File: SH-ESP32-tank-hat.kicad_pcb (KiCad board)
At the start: 2 copper layers, 34 x 58 mm, 50 parts, among them J301 I2C_top, J302 I2C_bottom, J303 GPIO subset, J304 Opto_bottom, J305 1-Wire_top, J306 1-Wire_bottom, J307 Opto_top, J401 Conn_01x02, J402 Conn_01x02, J501 Conn_01x02, Q401 S9015, Q402 S9015, U401 LMV324, U402 RCLAMP0524P-N, U403 RCLAMP0524P-N

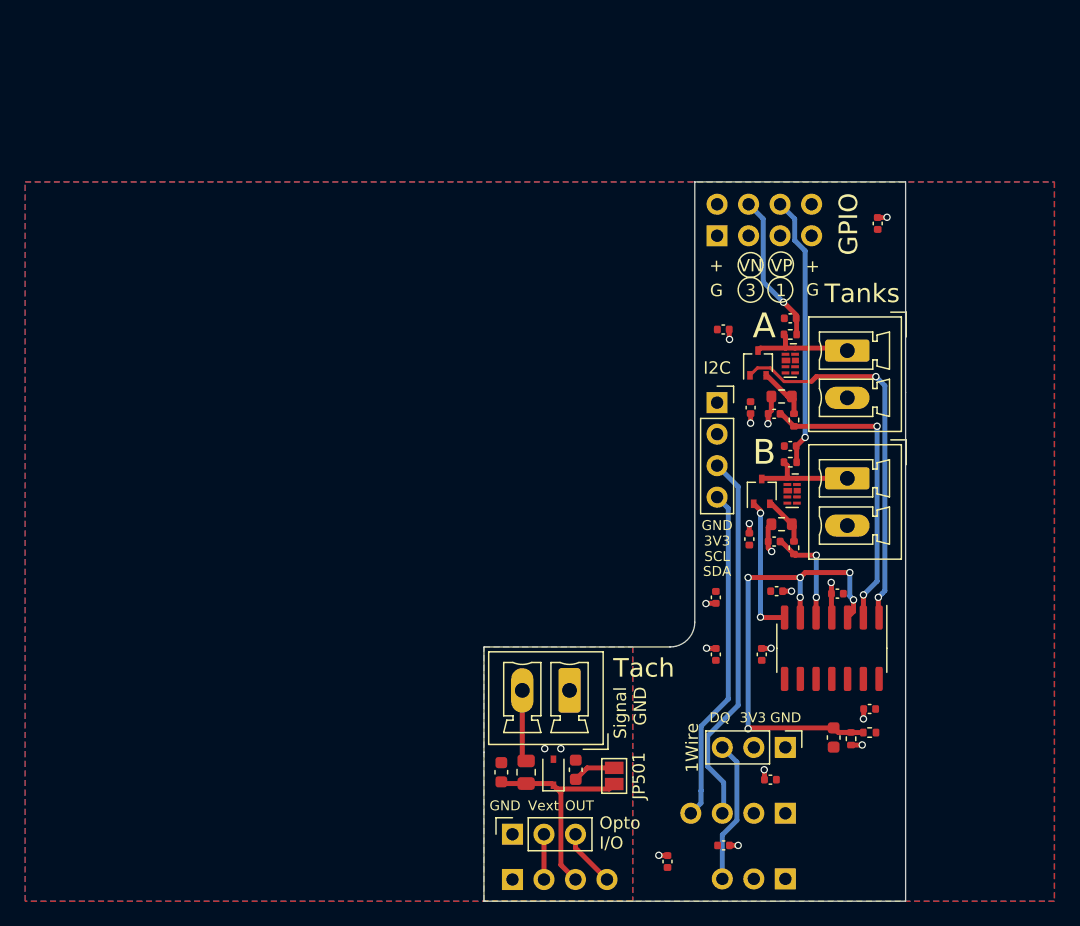
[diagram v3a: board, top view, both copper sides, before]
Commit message: Add 4x optocoupler input for alarms and other use
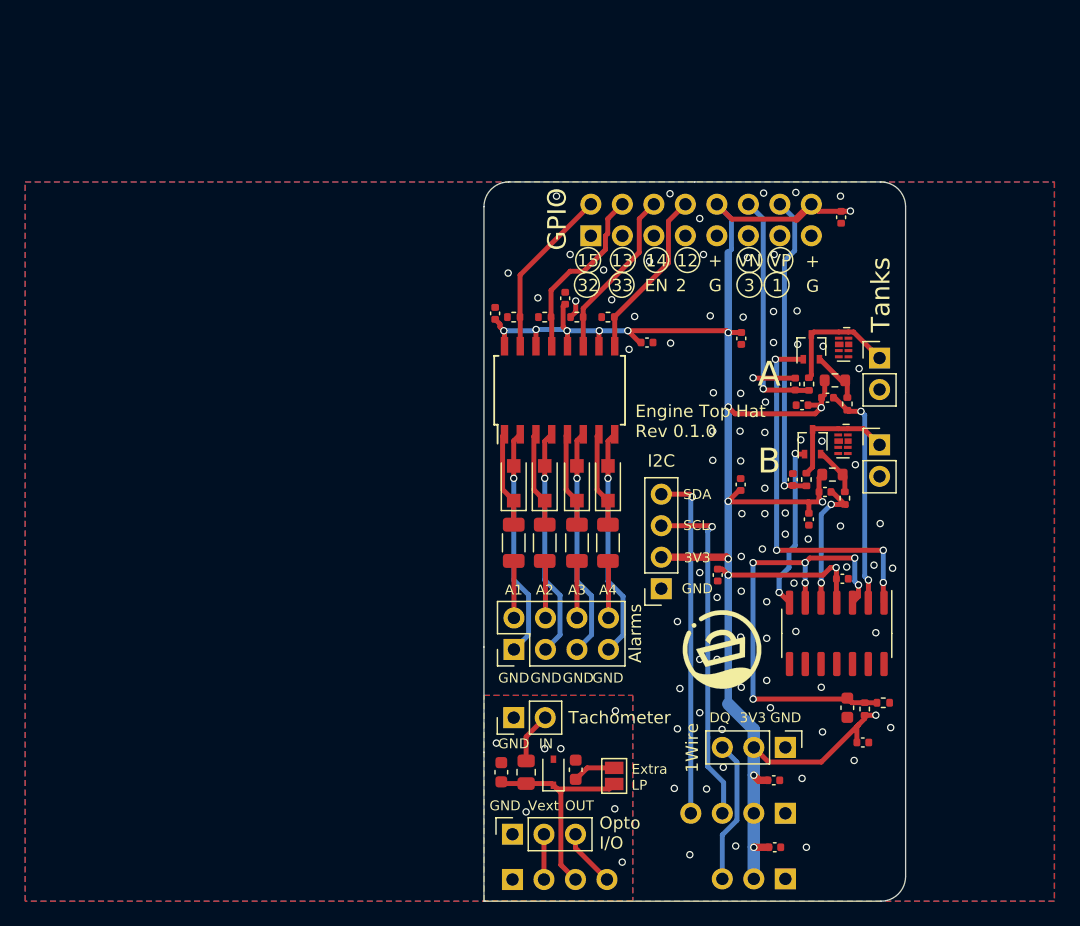
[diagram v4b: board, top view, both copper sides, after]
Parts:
- removed H201: MountingHole, SH-ESP32:MountingSlot_3.2mm_M3_Unplated
- added D601: SM4007PL, Diode_SMD:D_SOD-123F, F.Cu at (128.4, 81.3)
- added D602: SM4007PL, Diode_SMD:D_SOD-123F, F.Cu at (130.9, 81.3)
- added D603: SM4007PL, Diode_SMD:D_SOD-123F, F.Cu at (133.5, 81.3)
- added D604: SM4007PL, Diode_SMD:D_SOD-123F, F.Cu at (136.0, 81.3)
- added G***: LOGO, SH-ESP32-tank-hat:HL_pictogram_6.3mm, F.Cu at (145.2, 94.7)
- added G***: LOGO, SH-ESP32-tank-hat:Hat_Labs_20mm, B.Cu at (149.3, 94.9)
- added J601: Alarm input, Connector_PinHeader_2.54mm:PinHeader_2x04_P2.54mm_Vertical, F.Cu at (128.4, 94.7)
- added R601: 3.3k, Resistor_SMD:R_1206_3216Metric, F.Cu at (128.4, 86.1)
- added R602: 3.3k, Resistor_SMD:R_1206_3216Metric, F.Cu at (130.9, 86.1)
- added R603: 3.3k, Resistor_SMD:R_1206_3216Metric, F.Cu at (133.5, 86.1)
- added R604: 3.3k, Resistor_SMD:R_1206_3216Metric, F.Cu at (136.0, 86.1)
- added R605: 2.2k, Resistor_SMD:R_0402_1005Metric, F.Cu at (128.4, 67.9)
- added R606: 2.2k, Resistor_SMD:R_0402_1005Metric, F.Cu at (130.9, 67.9)
- added R607: 2.2k, Resistor_SMD:R_0402_1005Metric, F.Cu at (133.5, 67.9)
- added R608: 2.2k, Resistor_SMD:R_0402_1005Metric, F.Cu at (136.0, 67.9)
- added REF**: WEEE-Logo_5.6x8mm_SilkScreen, Symbol:WEEE-Logo_5.6x8mm_SilkScreen, B.Cu at (132.2, 73.6)
- added U601: ELQ3H7, Package_SO:SOIC-16W_5.3x10.2mm_P1.27mm, F.Cu at (132.1, 73.8)
- J303: footprint Connector_PinSocket_2.54mm:PinSocket_2x04_P2.54mm_Vertical -> Connector_PinSocket_2.54mm:PinSocket_2x08_P2.54mm_Vertical
- J401, J402, J501: footprint Connector_Phoenix_MC:PhoenixContact_MCV_1,5_2-G-3.81_1x02_P3.81mm_Vertical -> Connector_PinHeader_2.54mm:PinHeader_1x02_P2.54mm_Vertical
- moved C210 34.6 mm to (139.2, 70.0)
- moved C211 31.2 mm to (132.6, 66.4), turned to 270 degrees
- moved C207 27.2 mm to (152.2, 84.2), turned to 90 degrees
- moved REF** 25.7 mm to (132.2, 82.3)
- moved C212 22.0 mm to (126.9, 67.6)
- moved C201 20.4 mm to (151.7, 75.0), turned to 0 degrees
- moved J301 15.7 mm to (140.3, 89.8), turned to 180 degrees
- moved C205 14.0 mm to (156.6, 102.2), turned to 180 degrees
- moved G*** 13.1 mm to (132.2, 88.3)
- moved C209 10.8 mm to (149.4, 105.2), turned to 180 degrees
- moved J303 10.2 mm to (134.6, 61.3)
- moved C402 5.73 mm to (153.5, 82.0)
- moved Q402 5.73 mm to (152.5, 78.0)
- moved R402 5.73 mm to (155.1, 82.5)
- moved R404 5.73 mm to (154.1, 80.6)
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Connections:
- C405 pad 1: /IOHeader/ADC_A -> /Tank sender/ADC_A
- C406 pad 1: /IOHeader/ADC_B -> /Tank sender/ADC_B
- J303 pad 1: GND -> (no net)
- J303 pad 2: +3V3 -> /AL1
- J303 pad 4: /IOHeader/ADC_A -> /AL2
- J303 pad 6: /IOHeader/ADC_B -> /AL3
- J303 pad 7: GND -> (no net)
- J303 pad 8: +3V3 -> /AL4
- R407 pad 1: /IOHeader/ADC_A -> /Tank sender/ADC_A
- R408 pad 1: /IOHeader/ADC_B -> /Tank sender/ADC_B
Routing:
- net +3V3: track 17.7 -> 155.4 mm, vias 16 -> 17
- net /Tank sender/ADC_B: track 0.00 -> 25.3 mm, vias 0 -> 1
- net /IOHeader/ADC_B: track 22.0 -> 0.00 mm, vias 1 -> 0
- net /Tank sender/ADC_A: track 0.00 -> 19.1 mm, vias 0 -> 1
- net /Optocoupler input/GND2: track 0.00 -> 18.6 mm, vias 0 -> 1
- net /Optocoupler input/GND4: track 0.00 -> 18.6 mm, vias 0 -> 1
- net /Optocoupler input/GND1: track 0.00 -> 18.6 mm, vias 0 -> 1
- net /Optocoupler input/GND3: track 0.00 -> 18.5 mm, vias 0 -> 1
- net /AL2: track 0.00 -> 14.5 mm
- net /AL4: track 0.00 -> 13.8 mm
- net /AL1: track 0.00 -> 13.8 mm
- net /AL3: track 0.00 -> 13.8 mm
- net /IOHeader/ADC_A: track 12.1 -> 0.00 mm, vias 1 -> 0
- net Net-(D601-Pad1): track 0.00 -> 7.72 mm
- net Net-(D602-Pad1): track 0.00 -> 7.72 mm
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- added copper zone on B.Cu, net GND
- removed copper zone on B.Cu, net +3V3
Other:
- outline, holes or cut-outs redrawn
- board text added: "12"
- board text added: "13"
- board text added: "14"
- board text added: "15"
- board text added: "2"
- board text added: "32"
- board text added: "33"
- board text added: "A1"
- board text added: "A2"
- board text added: "A3"
- board text added: "A4"
- board text added: "Alarms"
- board text added: "EN"
- board text added: "Engine Top Hat Rev 0.1.0"
- board text added: "Extra LP"
- board text added: "IN"
- board text added: "Tachometer"
- board text removed: "Signal GND"
- board text removed: "Tach"
